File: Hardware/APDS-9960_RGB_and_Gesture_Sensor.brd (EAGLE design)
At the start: 160 x 100 mm, 18 parts, among them U1 APDS-9960

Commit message: Created initial layout
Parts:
- R3: value 22 -> 4.7k; device SparkFun-Resistors:0603-RES -> SparkFun-Resistors:0603
- R4: value 4.7k -> 22; device SparkFun-Resistors:0603 -> SparkFun-Resistors:0603-RES
- moved FRAME1 73.1 mm to (-7.62, -20.3)
- moved C2 48.7 mm to (7.62, 5.08), turned to 270 degrees
- moved C3 48.3 mm to (5.08, 15.2), turned to 270 degrees
- moved C1 47.2 mm to (3.81, 5.08), turned to 180 degrees
- moved SJ1 46.0 mm to (11.4, 5.08)
- moved STANDOFF1 43.3 mm to (2.54, 10.2)
- moved U1 43.3 mm to (7.62, 10.2)
- moved JP1 38.1 mm to (2.54, 1.27)
- moved R3 34.2 mm to (10.2, 15.2), turned to 270 degrees
- moved R2 33.0 mm to (12.7, 15.2), turned to 270 degrees
- moved R4 30.5 mm to (2.54, 15.2), turned to 270 degrees
- moved STANDOFF2 30.5 mm to (12.7, 10.2)
- moved R1 24.5 mm to (7.62, 15.2), turned to 90 degrees
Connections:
- net N$2: now also R3.2; no longer R4.2
- net N$3: now also R4.2; no longer R3.2
- net SCL: now also R3.1; no longer R4.1
- net VCC: now also R4.1; no longer R3.1
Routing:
- net VCC: track 0.00 -> 33.7 mm, vias 0 -> 2
- net SDA: track 0.00 -> 28.4 mm, vias 0 -> 1
- net SCL: track 0.00 -> 21.7 mm, vias 0 -> 2
- net INT: track 0.00 -> 18.1 mm, vias 0 -> 1
- net N$1: track 0.00 -> 13.3 mm
- net N$2: track 0.00 -> 10.8 mm
- net N$3: track 0.00 -> 9.02 mm
- net N$4: track 0.00 -> 0.97 mm
- added copper zone on layer 1, net GND
- added copper zone on layer 16, net GND
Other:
- board size 160 x 100 mm -> 15.2 x 17.8 mm
- board text added: "GND"

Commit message: Added SS text
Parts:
- U$1: value SFE_LOGO_NAME_WEB -> SFE_LOGO_NAME_FLAME.1_INCH; device SparkFun-Aesthetics:SFE-NEW-WEBLOGO -> SparkFun-Aesthetics:SFE_LOGO_NAME_FLAME_.1
- moved FID1 61.2 mm to (14.2, 2.79)
- moved FID2 47.4 mm to (1.02, 16.5)
- moved LOGO1 47.2 mm to (8.89, 6.10)
- moved U$1 43.5 mm to (11.4, 15.7), flipped to the bottom, turned to 270 degrees
- moved LOGO2 38.9 mm to (3.30, 14.0), flipped to the bottom
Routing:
- net SCL: track 21.7 -> 25.1 mm
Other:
- board text added: "APDS-9960"
- board text added: "I2C PU"
- board text added: "INT"
- board text added: "RGB/Gesture"
- board text added: "SCL"
- board text added: "SDA"
- board text added: "VCC"
- board text added: "v01"
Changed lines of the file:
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@@
 <setting verticaltext="up"/>
 </settings>
-<grid distance="0.001" unitdist="inch" unit="inch" style="dots" multiple="1" display="yes" altdistance="0.0001" altunitdist="inch" altunit="inch"/>
+<grid distance="0.01" unitdist="inch" unit="inch" style="dots" multiple="1" display="yes" altdistance="0.005" altunitdist="inch" altunit="inch"/>
 <layers>
 <layer number="1" name="Top" color="4" fill="1" visible="yes" active="yes"/>
 <layer number="2" name="Route2" color="1" fill="3" visible="no" active="yes"/>
 <layer number="15" name="Route15" color="4" fill="6" visible="no" active="yes"/>
-<layer number="16" name="Bottom" color="1" fill="1" visible="yes" active="yes"/>
+<layer number="16" name="Bottom" color="1" fill="1" visible="no" active="yes"/>
 <layer number="17" name="Pads" color="2" fill="1" visible="yes" active="yes"/>
 <layer number="18" name="Vias" color="2" fill="1" visible="yes" active="yes"/>
@@
 <layer number="20" name="Dimension" color="15" fill="1" visible="yes" active="yes"/>
 <layer number="21" name="tPlace" color="16" fill="1" visible="yes" active="yes"/>
-<layer number="22" name="bPlace" color="14" fill="1" visible="yes" active="yes"/>
+<layer number="22" name="bPlace" color="14" fill="1" visible="no" active="yes"/>
 <layer number="23" name="tOrigins" color="15" fill="1" visible="yes" active="yes"/>
-<layer number="24" name="bOrigins" color="15" fill="1" visible="yes" active="yes"/>
+<layer number="24" name="bOrigins" color="15" fill="1" visible="no" active="yes"/>
 <layer number="25" name="tNames" color="7" fill="1" visible="no" active="yes"/>
 <layer number="26" name="bNames" color="7" fill="1" visible="no" active="yes"/>
@@
 <layer number="43" name="vRestrict" color="2" fill="10" visible="no" active="yes"/>
 <layer number="44" name="Drills" color="7" fill="1" visible="no" active="yes"/>
-<layer number="45" name="Holes" color="7" fill="1" visible="yes" active="yes"/>
+<layer number="45" name="Holes" color="7" fill="1" visible="no" active="yes"/>
 <layer number="46" name="Milling" color="3" fill="1" visible="no" active="yes"/>
-<layer number="51" name="tDocu" color="6" fill="1" visible="yes" active="yes"/>
+<layer number="51" name="tDocu" color="6" fill="1" visible="no" active="yes"/>
 <layer number="52" name="bDocu" color="7" fill="1" visible="no" active="yes"/>
 <layer number="3" name="Route3" color="4" fill="3" visible="no" active="no"/>
@@
 <wire x1="15.24" y1="0" x2="15.24" y2="17.78" width="0.254" layer="20"/>
 <wire x1="15.24" y1="17.78" x2="0" y2="17.78" width="0.254" layer="20"/>
-<text x="-4.7244" y="3.1496" size="0.8128" layer="21" font="vector" ratio="15">GND</text>
+<text x="2.54" y="2.794" size="0.8128" layer="21" font="vector" ratio="15" align="bottom-center">GND</text>
+<text x="5.08" y="2.794" size="0.8128" layer="21" font="vector" ratio="15" align="bottom-center">VCC</text>
+<text x="7.62" y="2.794" size="0.8128" layer="21" font="vector" ratio="15" align="bottom-center">SDA</text>
+<text x="10.16" y="2.794" size="0.8128" layer="21" font="vector" ratio="15" align="bottom-center">SCL</text>
+<text x="12.7" y="2.794" size="0.8128" layer="21" font="vector" ratio="15" align="bottom-center">INT</text>
+<text x="2.54" y="2.794" size="0.8128" layer="22" font="vector" ratio="15" rot="MR0" align="bottom-center">GND</text>
+<text x="5.08" y="2.794" size="0.8128" layer="22" font="vector" ratio="15" rot="MR0" align="bottom-center">VCC</text>
+<text x="7.62" y="2.794" size="0.8128" layer="22" font="vector" ratio="15" rot="MR0" align="bottom-center">SDA</text>
+<text x="10.16" y="2.794" size="0.8128" layer="22" font="vector" ratio="15" rot="MR0" align="bottom-center">SCL</text>
+<text x="12.7" y="2.794" size="0.8128" layer="22" font="vector" ratio="15" rot="MR0" align="bottom-center">INT</text>
+<text x="13.97" y="14.224" size="1.2192" layer="16" font="vector" ratio="15" rot="SMR270" align="center">v01</text>
+<text x="4.318" y="5.334" size="0.8128" layer="22" font="vector" ratio="15" rot="MR0" align="bottom-center">APDS-9960</text>
+<text x="14.478" y="4.064" size="0.8128" layer="21" font="vector" ratio="15" rot="R90">I2C PU</text>
+<text x="4.318" y="4.318" size="0.8128" layer="22" font="vector" ratio="15" rot="MR0" align="bottom-center">RGB/Gesture</text>
 </plain>
 <attributes>
@@
 <attribute name="PROD_ID" value="CAP-00868" x="-12.7" y="-27.94" size="1.778" layer="27" rot="R270" display="off"/>
 </element>
-<element name="FID1" library="SparkFun-Aesthetics" package="FIDUCIAL-1X2" value="FIDUCIAL1X2" x="-43.18" y="24.13"/>
-<element name="FID2" library="SparkFun-Aesthetics" package="FIDUCIAL-1X2" value="FIDUCIAL1X2" x="-45.72" y="24.13"/>
+<element name="FID1" library="SparkFun-Aesthetics" package="FIDUCIAL-1X2" value="FIDUCIAL1X2" x="14.224" y="2.794"/>
+<element name="FID2" library="SparkFun-Aesthetics" package="FIDUCIAL-1X2" value="FIDUCIAL1X2" x="1.016" y="16.51"/>
 <element name="STANDOFF1" library="SparkFun-Electromechanical" package="STAND-OFF" value="STAND-OFF" x="2.54" y="10.16"/>
 <element name="STANDOFF2" library="SparkFun-Electromechanical" package="STAND-OFF" value="STAND-OFF" x="12.7" y="10.16"/>
-<element name="U$1" library="SparkFun-Aesthetics" package="SFE-NEW-WEBLOGO" value="SFE_LOGO_NAME_WEB" x="-31.75" y="10.16"/>
-<element name="LOGO1" library="SparkFun-Aesthetics" package="SFE_LOGO_FLAME_.1" value="SFE_LOGO_FLAME.1_INCH" x="-36.83" y="17.78"/>
-<element name="LOGO2" library="SparkFun-Aesthetics" package="OSHW-LOGO-S" value="OSHW-LOGOS" x="-34.29" y="24.13"/>
+<element name="U$1" library="SparkFun-Aesthetics" package="SFE_LOGO_NAME_FLAME_.1" value="SFE_LOGO_NAME_FLAME.1_INCH" x="11.43" y="15.748" rot="MR270"/>
+<element name="LOGO1" library="SparkFun-Aesthetics" package="SFE_LOGO_FLAME_.1" value="SFE_LOGO_FLAME.1_INCH" x="8.89" y="6.096"/>
+<element name="LOGO2" library="SparkFun-Aesthetics" package="OSHW-LOGO-S" value="OSHW-LOGOS" x="3.302" y="13.97" rot="MR0"/>
 <element name="R4" library="SparkFun-Resistors" package="0603-RES" value="22" x="2.54" y="15.24" rot="R270">
 <attribute name="PROD_ID" value="RES-08698" x="2.54" y="15.24" size="1.778" layer="27" font="vector" ratio="15" rot="R270" display="off"/>
@@
 </polygon>
 <via x="4.064" y="7.112" extent="1-16" drill="0.508"/>
-<via x="13.462" y="6.604" extent="1-16" drill="0.508"/>
-<via x="6.35" y="2.794" extent="1-16" drill="0.508"/>
+<via x="13.1064" y="6.8072" extent="1-16" drill="0.508"/>
+<via x="6.35" y="2.54" extent="1-16" drill="0.508"/>
+<via x="1.016" y="14.986" extent="1-16" drill="0.508"/>
+<via x="14.224" y="16.764" extent="1-16" drill="0.508"/>
 </signal>
 <signal name="VCC">
@@
 <wire x1="7.62" y1="16.256" x2="6.858" y2="17.018" width="0.254" layer="1"/>
 <via x="3.81" y="16.51" extent="1-16" drill="0.508"/>
-<via x="5.842" y="7.366" extent="1-16" drill="0.508"/>
-<wire x1="5.842" y1="7.366" x2="6.858" y2="7.366" width="0.381" layer="1"/>
-<wire x1="6.858" y1="7.366" x2="7.366" y2="7.366" width="0.381" layer="1"/>
-<wire x1="7.366" y1="7.366" x2="7.62" y2="7.112" width="0.381" layer="1"/>
-<wire x1="7.62" y1="7.112" x2="7.62" y2="5.93" width="0.381" layer="1"/>
-<wire x1="6.92" y1="8.705" x2="6.92" y2="7.428" width="0.381" layer="1"/>
-<wire x1="6.92" y1="7.428" x2="6.858" y2="7.366" width="0.254" layer="1"/>
+<via x="5.842" y="7.112" extent="1-16" drill="0.508"/>
 <wire x1="7.62" y1="5.93" x2="8.294" y2="5.93" width="0.254" layer="1"/>
 <wire x1="8.294" y1="5.93" x2="8.636" y2="5.588" width="0.254" layer="1"/>
@@
 <wire x1="11.176" y1="3.81" x2="9.144" y2="3.81" width="0.254" layer="1"/>
 <wire x1="9.144" y1="3.81" x2="8.636" y2="4.318" width="0.254" layer="1"/>
-<wire x1="5.842" y1="11.176" x2="5.842" y2="7.366" width="0.254" layer="16"/>
+<wire x1="5.842" y1="11.176" x2="5.842" y2="7.112" width="0.254" layer="16"/>
 <wire x1="3.81" y1="16.51" x2="3.81" y2="13.208" width="0.254" layer="16"/>
 <wire x1="3.81" y1="13.208" x2="5.842" y2="11.176" width="0.254" layer="16"/>
@@
 <wire x1="2.628" y1="16.002" x2="3.302" y2="16.002" width="0.254" layer="1"/>
 <wire x1="3.302" y1="16.002" x2="3.81" y2="16.51" width="0.254" layer="1"/>
+<wire x1="7.62" y1="5.93" x2="7.62" y2="6.858" width="0.381" layer="1"/>
+<wire x1="7.62" y1="6.858" x2="7.366" y2="7.112" width="0.381" layer="1"/>
+<wire x1="7.366" y1="7.112" x2="6.858" y2="7.112" width="0.381" layer="1"/>
+<wire x1="6.858" y1="7.112" x2="5.842" y2="7.112" width="0.381" layer="1"/>
+<wire x1="6.92" y1="8.705" x2="6.92" y2="7.174" width="0.381" layer="1"/>
+<wire x1="6.92" y1="7.174" x2="6.858" y2="7.112" width="0.381" layer="1"/>
 </signal>
 <signal name="SCL">
@@
 <wire x1="6.373" y1="10.645" x2="5.9436" y2="11.0744" width="0.254" layer="1"/>
 <wire x1="10.16" y1="1.27" x2="8.382" y2="3.048" width="0.254" layer="16"/>
-<wire x1="8.382" y1="3.048" x2="8.382" y2="10.795" width="0.254" layer="16"/>
 <wire x1="5.9436" y1="13.1826" x2="5.9436" y2="11.0744" width="0.254" layer="1"/>
 <wire x1="9.906" y1="14.478" x2="7.239" y2="14.478" width="0.254" layer="16"/>
 <wire x1="7.239" y1="14.478" x2="5.9436" y2="13.1826" width="0.254" layer="16"/>
-<wire x1="8.382" y1="10.795" x2="6.92" y2="10.645" width="0" layer="19" extent="1-16"/>
+<wire x1="8.382" y1="3.048" x2="8.382" y2="10.7442" width="0.254" layer="16"/>
+<wire x1="8.382" y1="10.7442" x2="5.9436" y2="13.1826" width="0.254" layer="16"/>
 </signal>
 <signal name="SDA">

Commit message: Added name on layout
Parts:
- moved FRAME1 19.4 mm to (-24.1, -10.2)
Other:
- board text added: "Shawn Hymel"
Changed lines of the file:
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@@
 <setting verticaltext="up"/>
 </settings>
-<grid distance="0.01" unitdist="inch" unit="inch" style="dots" multiple="1" display="yes" altdistance="0.005" altunitdist="inch" altunit="inch"/>
+<grid distance="0.05" unitdist="inch" unit="inch" style="dots" multiple="1" display="yes" altdistance="0.005" altunitdist="inch" altunit="inch"/>
 <layers>
 <layer number="1" name="Top" color="4" fill="1" visible="yes" active="yes"/>
 <layer number="2" name="Route2" color="1" fill="3" visible="no" active="yes"/>
 <layer number="15" name="Route15" color="4" fill="6" visible="no" active="yes"/>
-<layer number="16" name="Bottom" color="1" fill="1" visible="no" active="yes"/>
+<layer number="16" name="Bottom" color="1" fill="1" visible="yes" active="yes"/>
 <layer number="17" name="Pads" color="2" fill="1" visible="yes" active="yes"/>
 <layer number="18" name="Vias" color="2" fill="1" visible="yes" active="yes"/>
@@
 <layer number="20" name="Dimension" color="15" fill="1" visible="yes" active="yes"/>
 <layer number="21" name="tPlace" color="16" fill="1" visible="yes" active="yes"/>
-<layer number="22" name="bPlace" color="14" fill="1" visible="no" active="yes"/>
+<layer number="22" name="bPlace" color="14" fill="1" visible="yes" active="yes"/>
 <layer number="23" name="tOrigins" color="15" fill="1" visible="yes" active="yes"/>
-<layer number="24" name="bOrigins" color="15" fill="1" visible="no" active="yes"/>
+<layer number="24" name="bOrigins" color="15" fill="1" visible="yes" active="yes"/>
 <layer number="25" name="tNames" color="7" fill="1" visible="no" active="yes"/>
 <layer number="26" name="bNames" color="7" fill="1" visible="no" active="yes"/>
@@
 <layer number="43" name="vRestrict" color="2" fill="10" visible="no" active="yes"/>
 <layer number="44" name="Drills" color="7" fill="1" visible="no" active="yes"/>
-<layer number="45" name="Holes" color="7" fill="1" visible="no" active="yes"/>
+<layer number="45" name="Holes" color="7" fill="1" visible="yes" active="yes"/>
 <layer number="46" name="Milling" color="3" fill="1" visible="no" active="yes"/>
-<layer number="51" name="tDocu" color="6" fill="1" visible="no" active="yes"/>
+<layer number="51" name="tDocu" color="6" fill="1" visible="yes" active="yes"/>
 <layer number="52" name="bDocu" color="7" fill="1" visible="no" active="yes"/>
 <layer number="3" name="Route3" color="4" fill="3" visible="no" active="no"/>
@@
 <text x="14.478" y="4.064" size="0.8128" layer="21" font="vector" ratio="15" rot="R90">I2C PU</text>
 <text x="4.318" y="4.318" size="0.8128" layer="22" font="vector" ratio="15" rot="MR0" align="bottom-center">RGB/Gesture</text>
+<text x="7.62" y="-10.16" size="1.778" layer="51" font="vector">Shawn Hymel</text>
 </plain>
 <attributes>
@@
 </autorouter>
 <elements>
-<element name="FRAME1" library="SparkFun-Aesthetics" package="CREATIVE_COMMONS" value="FRAME-LETTER" x="-7.62" y="-20.32"/>
+<element name="FRAME1" library="SparkFun-Aesthetics" package="CREATIVE_COMMONS" value="FRAME-LETTER" x="-24.13" y="-10.16"/>
 <element name="U1" library="SparkFun-Sensors" package="APDS-9960" value="APDS-9960" x="7.62" y="10.16">
 <attribute name="PROD_ID" value="SEN-12005" x="43.18" y="-2.54" size="1.778" layer="27" display="off"/>

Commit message: Replaced 4.7k INT pullup with 10k
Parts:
- R1: value 4.7k -> 10k; device SparkFun-Resistors:0603 -> SparkFun-Resistors:0603-RES
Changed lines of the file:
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@@
 </element>
 <element name="JP1" library="SparkFun-Connectors" package="1X05" value="" x="2.54" y="1.27"/>
-<element name="R1" library="SparkFun-Resistors" package="0603" value="4.7k" x="7.62" y="15.24" rot="R90">
-<attribute name="PROD_ID" value="RES-07857" x="31.75" y="30.48" size="1.778" layer="27" rot="R90" display="off"/>
+<element name="R1" library="SparkFun-Resistors" package="0603-RES" value="10k" x="7.62" y="15.24" rot="R90">
+<attribute name="PROD_ID" value="RES-00824" x="31.75" y="30.48" size="1.778" layer="27" rot="R90" display="off"/>
+<attribute name="VALUE" value="10K" x="7.62" y="15.24" size="1.778" layer="27" rot="R90" display="off"/>
 </element>
 <element name="R2" library="SparkFun-Resistors" package="0603" value="4.7k" x="12.7" y="15.24" rot="R270">

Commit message: Rotated OSHW logo and added I2C address to sch and silk.
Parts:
- moved U$1 0.25 mm to (11.7, 15.7)
- turned LOGO2 to 270 degrees
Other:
- board text added: "I2C: 0x39"
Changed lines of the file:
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@@
 <text x="4.318" y="4.318" size="0.8128" layer="22" font="vector" ratio="15" rot="MR0" align="bottom-center">RGB/Gesture</text>
 <text x="7.62" y="-10.16" size="1.778" layer="51" font="vector">Shawn Hymel</text>
+<text x="7.62" y="16.51" size="0.8128" layer="22" font="vector" ratio="15" rot="MR0" align="bottom-center">I2C: 0x39</text>
 </plain>
 <attributes>
@@
 <element name="STANDOFF1" library="SparkFun-Electromechanical" package="STAND-OFF" value="STAND-OFF" x="2.54" y="10.16"/>
 <element name="STANDOFF2" library="SparkFun-Electromechanical" package="STAND-OFF" value="STAND-OFF" x="12.7" y="10.16"/>
-<element name="U$1" library="SparkFun-Aesthetics" package="SFE_LOGO_NAME_FLAME_.1" value="SFE_LOGO_NAME_FLAME.1_INCH" x="11.43" y="15.748" rot="MR270"/>
+<element name="U$1" library="SparkFun-Aesthetics" package="SFE_LOGO_NAME_FLAME_.1" value="SFE_LOGO_NAME_FLAME.1_INCH" x="11.684" y="15.748" rot="MR270"/>
 <element name="LOGO1" library="SparkFun-Aesthetics" package="SFE_LOGO_FLAME_.1" value="SFE_LOGO_FLAME.1_INCH" x="8.89" y="6.096"/>
-<element name="LOGO2" library="SparkFun-Aesthetics" package="OSHW-LOGO-S" value="OSHW-LOGOS" x="3.302" y="13.97" rot="MR0"/>
+<element name="LOGO2" library="SparkFun-Aesthetics" package="OSHW-LOGO-S" value="OSHW-LOGOS" x="3.302" y="13.97" rot="MR270"/>
 <element name="R4" library="SparkFun-Resistors" package="0603-RES" value="22" x="2.54" y="15.24" rot="R270">
 <attribute name="PROD_ID" value="RES-08698" x="2.54" y="15.24" size="1.778" layer="27" font="vector" ratio="15" rot="R270" display="off"/>

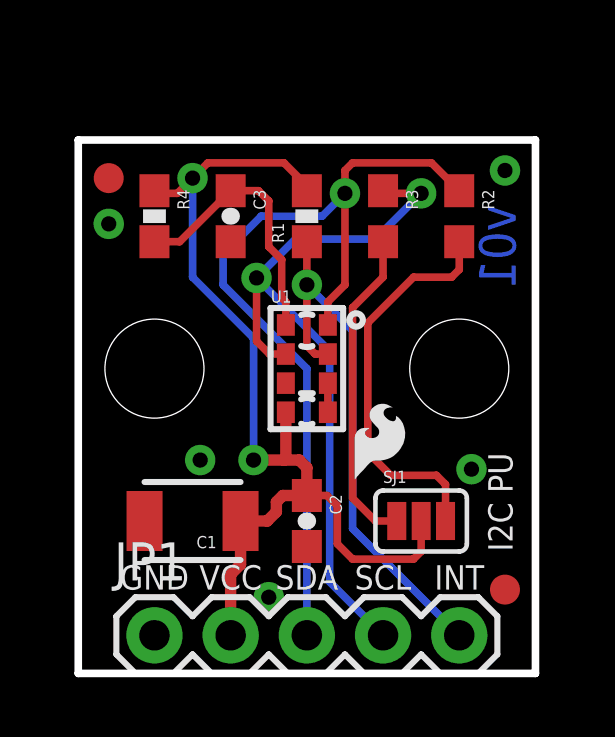
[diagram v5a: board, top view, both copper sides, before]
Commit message: Added separate VLED (VL) pin, connected VL and VCC with solder jumper and optional resistor. Re-did layout to support new features.
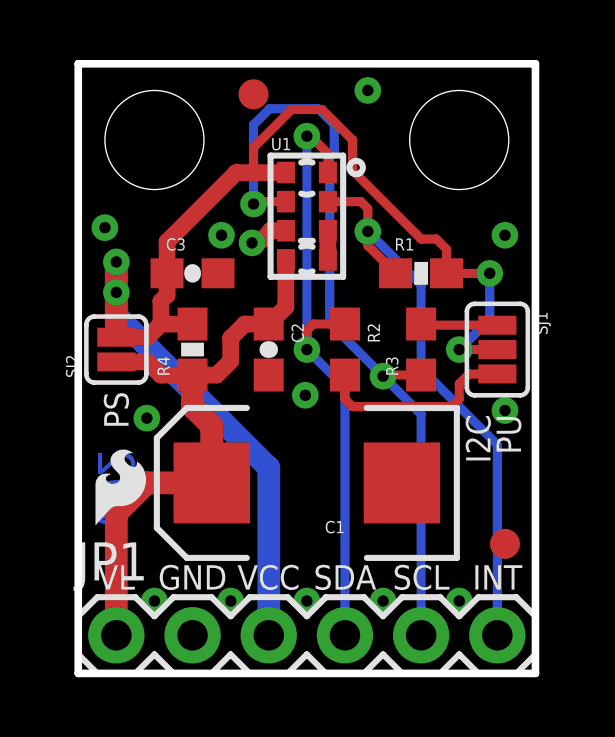
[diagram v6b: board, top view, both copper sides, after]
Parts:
- added SJ2: SOLDERJUMPERNC, SparkFun-Retired:SJ_2S
- C1: value 10uF -> 100uF; device SparkFun-Capacitors:1210 -> SparkFun-Capacitors:EIA7343
- JP1: device SparkFun-Connectors:1X05 -> SparkFun-Connectors:1X06
- R4: value 22 -> DNP
- moved U$1 11.6 mm to (13.6, 4.32), turned to 0 degrees
- moved LOGO1 8.77 mm to (0.25, 4.57)
- moved STANDOFF1 7.62 mm to (2.54, 17.8)
- moved STANDOFF2 7.62 mm to (12.7, 17.8)
- moved SJ1 6.25 mm to (14.0, 10.8), turned to 270 degrees
- moved C2 5.85 mm to (6.35, 10.8)
- moved R2 5.85 mm to (8.89, 10.8)
- moved LOGO2 5.76 mm to (7.62, 17.8), turned to 0 degrees
- moved FID2 5.58 mm to (5.84, 19.3)
- moved U1 5.08 mm to (7.62, 15.2)
- moved R3 4.62 mm to (11.4, 10.8), turned to 90 degrees
- moved R4 4.62 mm to (3.81, 10.8), turned to 90 degrees
- moved R1 4.26 mm to (11.4, 13.3), turned to 0 degrees
- moved C1 4.02 mm to (7.62, 6.35)
- moved C3 2.29 mm to (3.81, 13.3), turned to 0 degrees
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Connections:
- removed net N$3: C3.1, R4.2, U1.8
- new net VL: C1.A, C2.1, JP1.1, R4.1, SJ2.1, U1.5
- net GND: now also C1.C, JP1.2; no longer C1.2, JP1.1
- net INT: now also JP1.6; no longer JP1.5
- net SCL: now also JP1.5; no longer JP1.4
- net SDA: now also JP1.4; no longer JP1.3
- net VCC: now also C3.1, JP1.3, R4.2, SJ2.2, U1.8; no longer C1.1, C2.1, JP1.2, R4.1, U1.5
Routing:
- net VL: track 0.00 -> 20.3 mm
- net VCC: track 33.9 -> 44.3 mm, vias 2 -> 4
- net N$3: track 9.02 -> 0.00 mm
- net N$2: track 10.8 -> 2.56 mm
- net SDA: track 28.4 -> 20.7 mm, vias 1 -> 2
- net N$1: track 13.3 -> 6.74 mm
- net SCL: track 25.1 -> 26.5 mm
- net INT: track 18.1 -> 19.2 mm
- net GND: track 0.00 -> 1.00 mm, vias 5 -> 13
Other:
- board size 15.2 x 17.8 mm -> 15.2 x 20.3 mm
- board text added: "I2C"
- board text added: "PS"
- board text added: "PU"
- board text added: "VL"
- board text added: "v02"
- board text removed: "I2C PU"
- board text removed: "v01"

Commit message: Updated version number to v10 for reds
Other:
- board text added: "v10"
- board text removed: "v02"
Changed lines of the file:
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@@
 <text x="11.43" y="2.794" size="0.8128" layer="22" font="vector" ratio="15" rot="MR0" align="bottom-center">SCL</text>
 <text x="13.97" y="2.794" size="0.8128" layer="22" font="vector" ratio="15" rot="MR0" align="bottom-center">INT</text>
-<text x="1.27" y="6.096" size="1.2192" layer="16" font="vector" ratio="15" rot="SMR90" align="center">v02</text>
+<text x="1.27" y="6.096" size="1.2192" layer="16" font="vector" ratio="15" rot="SMR90" align="center">v10</text>
 <text x="7.62" y="12.954" size="0.8128" layer="22" font="vector" ratio="15" rot="MR0" align="bottom-center">APDS-9960</text>
 <text x="13.335" y="8.636" size="0.8128" layer="21" font="vector" ratio="15" rot="R90" align="center-right">I2C</text>
